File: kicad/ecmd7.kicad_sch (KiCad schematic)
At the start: 91 parts, among them J1 PMOD_SPI_ENC, J2 PMOD_ADC_MPIO, J3 PMOD_DRV, J4 Conn_01x02_Socket, J5 Encoder, J6 12V, J7 RS422/BISS-C, J8 5V, Q1 IRFS3806, Q11 MMBT3904, Q12 MMBT3904, Q2 IRFS3806, Q3 IRFS3806, Q4 IRFS3806, Q5 IRFS3806, Q6 IRFS3806, U1 TMC6200-TA

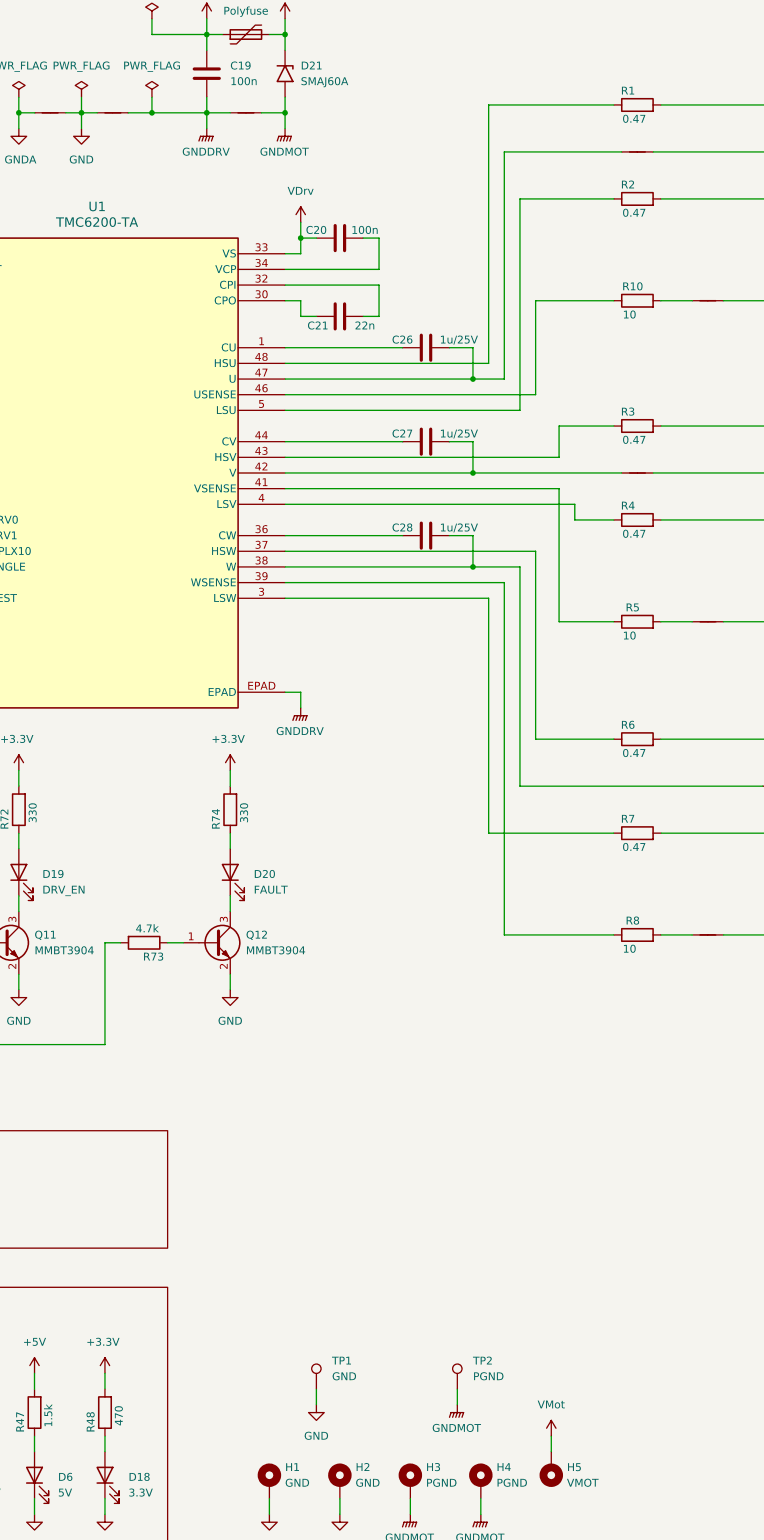
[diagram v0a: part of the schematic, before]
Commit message: Update project structure for enhancment with firmware and software
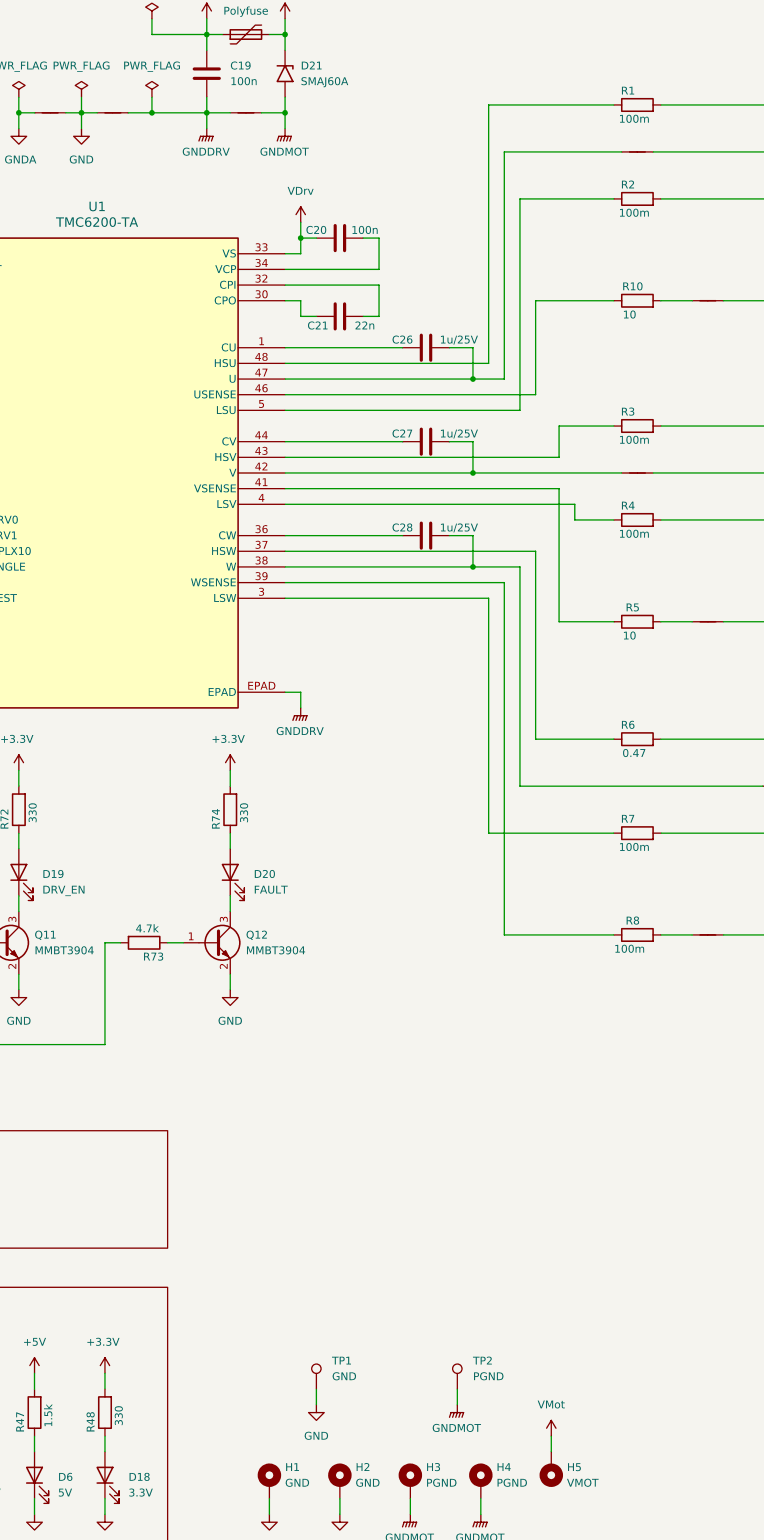
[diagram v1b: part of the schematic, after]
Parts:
- D21: Mouser Part Number (none) -> 576-SMAJ60A
- R1, R2, R3, R4, R7: value 0.47 -> 100m
- R48: value 470 -> 330
- R8: value 10 -> 100m
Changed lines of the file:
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@@
 			)
 		)
-		(property "Value" "0.47"
+		(property "Value" "100m"
 			(at 301.752 58.166 90)
 			(effects
@@
 			)
 		)
-		(property "Value" "0.47"
+		(property "Value" "100m"
 			(at 301.752 94.996 90)
 			(effects
@@
 			)
 		)
-		(property "Value" "0.47"
+		(property "Value" "100m"
 			(at 301.752 161.036 90)
 			(effects
@@
 			)
 		)
+		(property "Mouser Part Number" " 576-SMAJ60A"
+			(at 245.11 35.56 90)
+			(effects
+				(font
+					(size 1.27 1.27)
+				)
+				(hide yes)
+			)
+		)
 		(pin "1"
 		)
@@
 			)
 		)
-		(property "Value" "0.47"
+		(property "Value" "100m"
 			(at 301.752 42.926 90)
 			(effects
@@
 			)
 		)
-		(property "Value" "10"
+		(property "Value" "100m"
 			(at 300.99 177.546 90)
 			(effects
@@
 			)
 		)
-		(property "Value" "470"
+		(property "Value" "330"
 			(at 218.186 253.238 90)
 			(effects
@@
 			)
 		)
-		(property "Value" "0.47"
+		(property "Value" "100m"
 			(at 301.752 110.236 90)
 			(effects

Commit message: Cleanup schematic
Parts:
- removed C13, C14, C15, C16, C17, C18: 1n, Capacitor_SMD:C_0805_2012Metric, symbol Device:C
- removed C19, C20, C22, C25: 100n, Capacitor_SMD:C_0805_2012Metric, symbol Device:C
- removed C21: 22n, Capacitor_SMD:C_0805_2012Metric, symbol Device:C
- removed C23: 4.7u/25V, Capacitor_SMD:C_0805_2012Metric, symbol Device:C
- removed C24: 2.2u/25V, Capacitor_SMD:C_0805_2012Metric, symbol Device:C
- removed C26, C27, C28: 1u/25V, Capacitor_SMD:C_0805_2012Metric, symbol Device:C
- removed D18: 3.3V, Diode_SMD:D_0805_2012Metric, symbol Device:LED
- removed D19: DRV_EN, Diode_SMD:D_0805_2012Metric, symbol Device:LED
- removed D20: FAULT, Diode_SMD:D_0805_2012Metric, symbol Device:LED
- removed D21: SMAJ60A, Diode_SMD:D_SMA, symbol Diode:SMAJ60A
- removed D5: 12V, Diode_SMD:D_0805_2012Metric, symbol Device:LED
- removed D6: 5V, Diode_SMD:D_0805_2012Metric, symbol Device:LED
- removed F1: Polyfuse, Fuse:Fuse_0805_2012Metric, symbol Device:Polyfuse
- removed J6: 12V, Connector_PinSocket_2.54mm:PinSocket_1x02_P2.54mm_Vertical, symbol Connector:Conn_01x02_Socket
- removed J8: 5V, Connector_PinSocket_2.54mm:PinSocket_1x02_P2.54mm_Vertical, symbol Connector:Conn_01x02_Socket
- removed NTP2G1, NTP2G4: NetTie_2, NetTie:NetTie-2_SMD_Pad2.0mm, symbol Device:NetTie_2
- removed NTP2G2, NTPU1, NTPV1, NTPW1, NTSU1, NTSV1, NTSW1: NetTie_2, NetTie:NetTie-2_SMD_Pad0.5mm, symbol Device:NetTie_2
- removed Q1, Q2, Q3, Q4, Q5, Q6: IRFS3806, Package_TO_SOT_SMD:TO-263-2, symbol Transistor_FET:IRFS4115
- removed Q11, Q12: MMBT3904, Package_TO_SOT_SMD:SOT-23, symbol Transistor_BJT:MMBT3904
- removed R1, R2, R3, R4, R7, R8: 100m, Resistor_SMD:R_0805_2012Metric, symbol Device:R
- removed R10, R5: 10, Resistor_SMD:R_0805_2012Metric, symbol Device:R
- removed R46, R69, R73: 4.7k, Resistor_SMD:R_0805_2012Metric, symbol Device:R
- removed R47: 1.5k, Resistor_SMD:R_0805_2012Metric, symbol Device:R
- removed R48, R72, R74: 330, Resistor_SMD:R_0805_2012Metric, symbol Device:R
- removed R6: 0.47, Resistor_SMD:R_0805_2012Metric, symbol Device:R
- removed RU1, RV1, RW1: 15m, Resistor_SMD:R_0612_1632Metric, symbol Device:R
- removed TPU1: U, TestPoint:TestPoint_Loop_D2.50mm_Drill1.0mm, symbol Connector:TestPoint
- removed TPV1: V, TestPoint:TestPoint_Loop_D2.50mm_Drill1.0mm, symbol Connector:TestPoint
- removed TPW1: W, TestPoint:TestPoint_Loop_D2.50mm_Drill1.0mm, symbol Connector:TestPoint
- removed U1: TMC6200-TA, SSTA:eTQFP48_9x9_TRI, symbol SSTA:TMC6200-TA
- added C76: 100n, Capacitor_SMD:C_0805_2012Metric, symbol Device:C
- added JP10: ~{WP}=1, Jumper:SolderJumper-2_P1.3mm_Bridged_RoundedPad1.0x1.5mm, symbol Jumper:SolderJumper_2_Bridged
- added JP12: ~{WP}=0, Jumper:SolderJumper-2_P1.3mm_Open_RoundedPad1.0x1.5mm, symbol Jumper:SolderJumper_2_Open
- added R49, R53, R76, R9: 4.7k, Resistor_SMD:R_0805_2012Metric, symbol Device:R
- added U15: 74LVC1G139, Package_SO:SSOP-8_2.95x2.8mm_P0.65mm, symbol 74xGxx:74LVC1G139
- added U16: MB85RS1MT, Package_SO:SOP-8_3.76x4.96mm_P1.27mm, symbol Memory_NVRAM:MB85RS1MT
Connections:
- net +3.3V: now also C76.1, JP10.2 (B), R53.1, R9.1, U15.8 (VCC), U16.8 (VDD)
- net CS0: now also U15.1 (A)
- net CS1: now also U15.2 (B)
- net GND: now also C76.2, JP12.1 (A), R49.2, R76.2, U15.4 (GND), U16.4 (GND), U16.7 (~{HOLD})
- net SPI_SCK: now also R53.2, R76.1, U16.6 (SCK)
- net SPI_SDI: now also R49.1, R9.2, U16.5 (SI)
- net SPI_SDO: now also U16.2 (SO)
- net ~{CS_DRV}: now also U15.6 (Y1)
- net Power Stage/U: now reaches JU1.1 (Pin_1)
- net Power Stage/W: now reaches JW1.1 (Pin_1)
- net Power Stage/V: now reaches JV1.1 (Pin_1)
- new net: JP10.1 (A), JP12.2 (B), U16.3 (~{WP})
- new net ~{CS_FRAM}: U15.5 (Y2), U16.1 (~{CS})
- new net ~{CS_TMP}: U15.3 (Y3)
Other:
- sheet ADC+IO renamed ADC
- added sheet Power Stage (powerstage.kicad_sch)
- added sheet Sensors (sensors.kicad_sch)
- sheet ADC ports: added AD_SCK, AD_SDO_IU, AD_SDO_IV, AD_SDO_IW, AD_SDO_VBUS, I_U, I_V, I_W, ~{CS_AD}; removed none
- note added: "ABZ-Encoder Supply Selection"
- note added: "Battery/Power Connector"
- note added: "BiSS-C/RS422 Supply Selection"
- note added: "Control Connectors"
- note added: "Controller"
- note added: "Motor Terminals"
- note added: "SPI 2-to-4 CS Decoder"
- note added: "SPI FRAM (Nonvolatile Config Memory)"
- note added: "SPI Pseudo Termination"
- moved on the sheet: C42, C57, F2, F3, H1, H2, H3, H4, H5, J1, J2, J3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

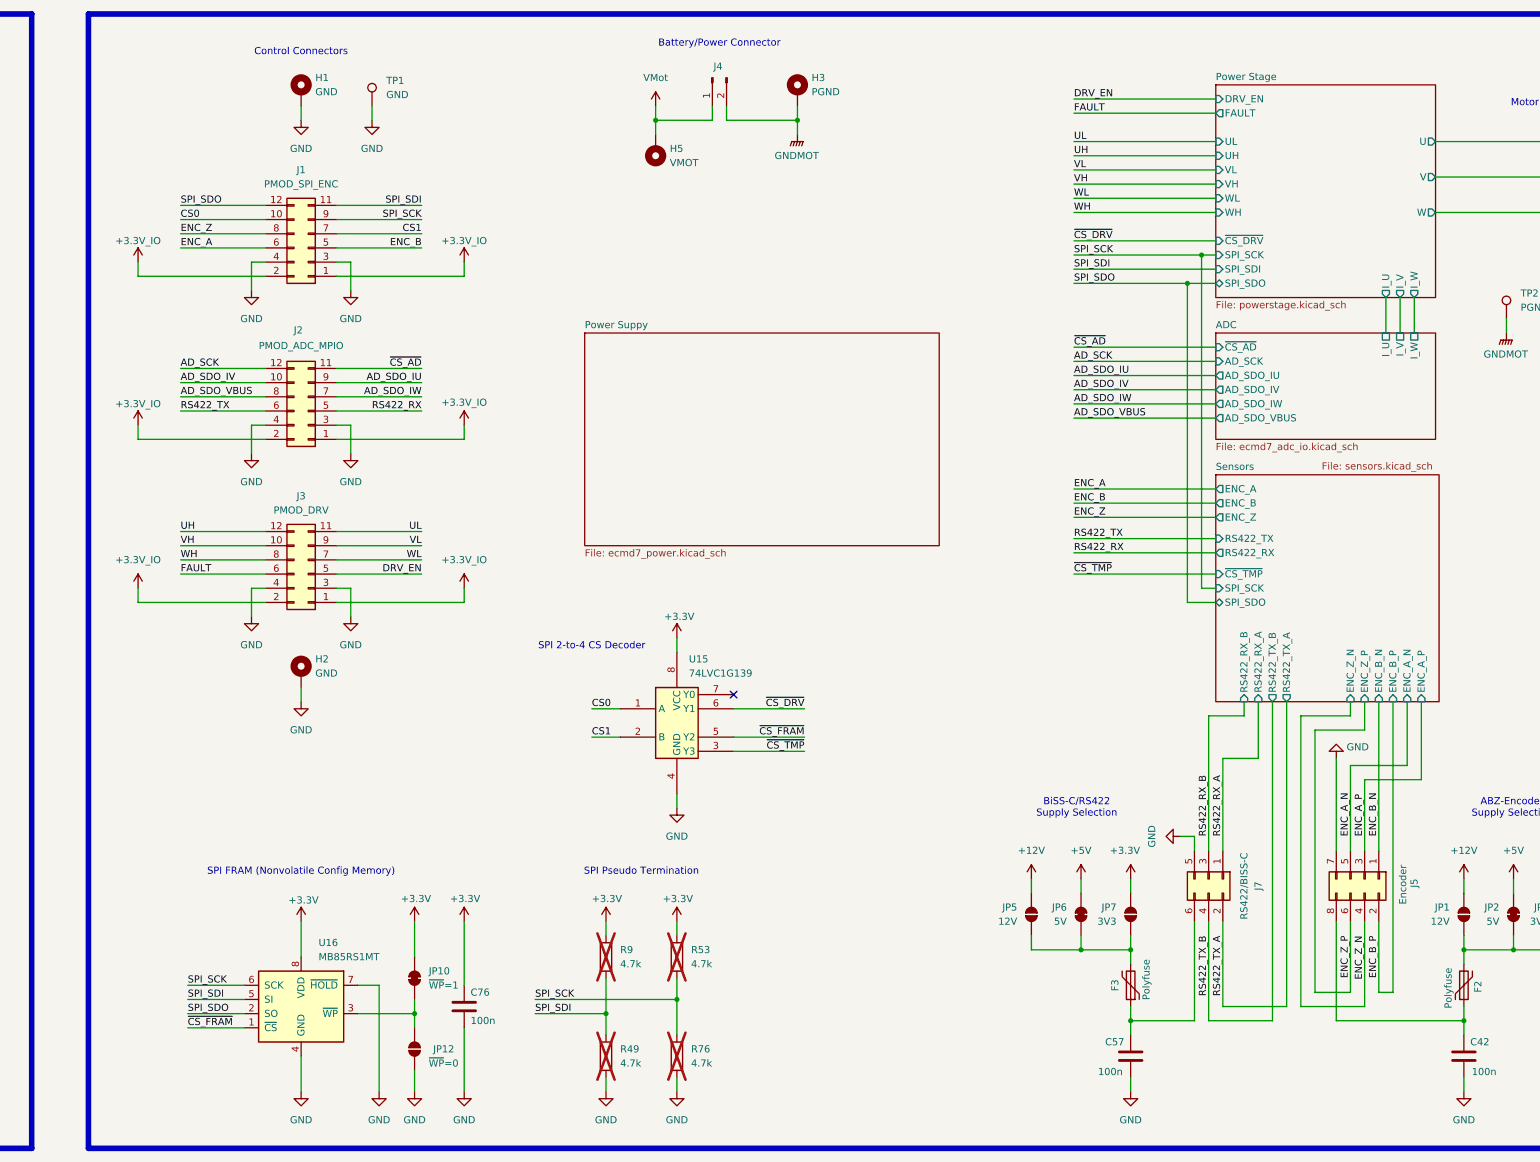
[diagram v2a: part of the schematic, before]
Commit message: Cleanup schematic, add busses
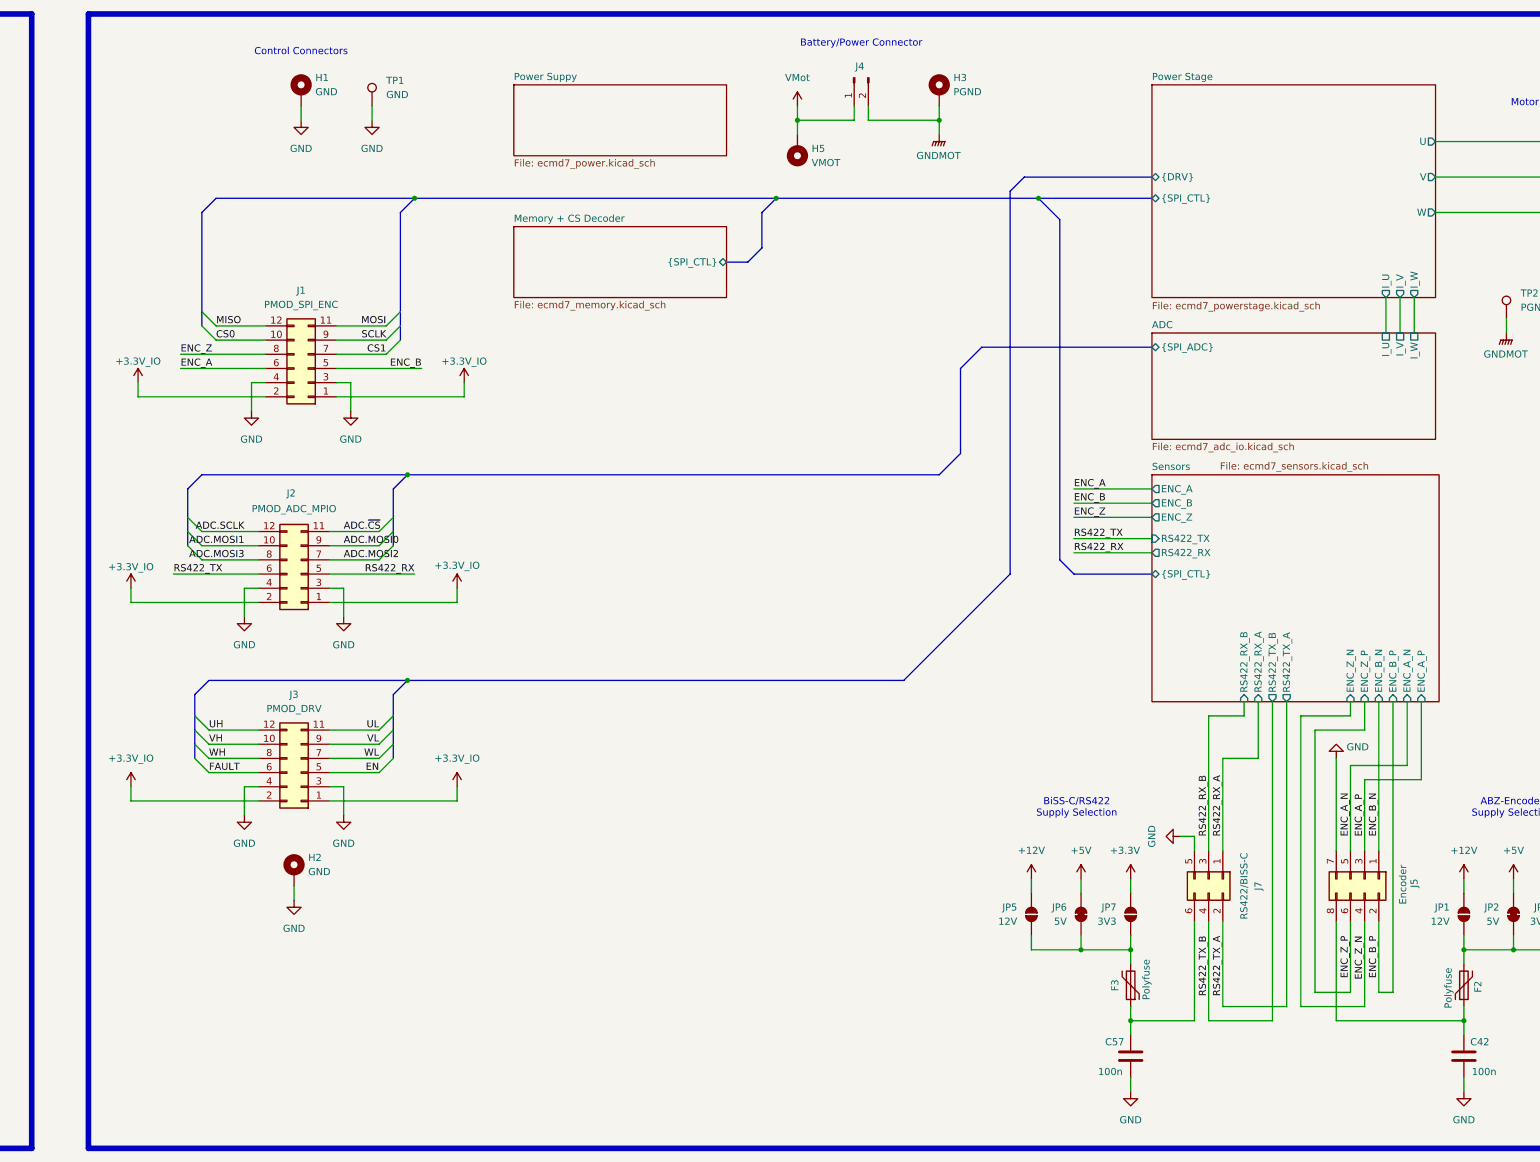
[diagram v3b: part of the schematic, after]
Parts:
- removed C76: 100n, Capacitor_SMD:C_0805_2012Metric, symbol Device:C
- removed JP10: ~{WP}=1, Jumper:SolderJumper-2_P1.3mm_Bridged_RoundedPad1.0x1.5mm, symbol Jumper:SolderJumper_2_Bridged
- removed JP12: ~{WP}=0, Jumper:SolderJumper-2_P1.3mm_Open_RoundedPad1.0x1.5mm, symbol Jumper:SolderJumper_2_Open
- removed R49, R53, R76, R9: 4.7k, Resistor_SMD:R_0805_2012Metric, symbol Device:R
- removed U15: 74LVC1G139, Package_SO:SSOP-8_2.95x2.8mm_P0.65mm, symbol 74xGxx:74LVC1G139
- removed U16: MB85RS1MT, Package_SO:SOP-8_3.76x4.96mm_P1.27mm, symbol Memory_NVRAM:MB85RS1MT
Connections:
- net AD_SCK renamed ADC.SCLK
- net AD_SDO_IU renamed ADC.MOSI0
- net AD_SDO_IV renamed ADC.MOSI1
- net AD_SDO_IW renamed ADC.MOSI2
- net AD_SDO_VBUS renamed ADC.MOSI3
- net DRV_EN renamed EN
- net SPI_SCK renamed SCLK
- net SPI_SDI renamed MOSI
- net SPI_SDO renamed MISO
- net ~{CS_AD} renamed ADC.~{CS}
- no-connect marks 1 -> 0
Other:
- added sheet Memory + CS Decoder (ecmd7_memory.kicad_sch)
- sheet ADC ports: added {SPI_ADC}; removed AD_SCK, AD_SDO_IU, AD_SDO_IV, AD_SDO_IW, AD_SDO_VBUS, ~{CS_AD}
- sheet Power Stage: file powerstage.kicad_sch -> ecmd7_powerstage.kicad_sch
- sheet Power Stage ports: added {DRV}, {SPI_CTL}; removed DRV_EN, FAULT, SPI_SCK, SPI_SDI, SPI_SDO, UH, UL, VH, VL, WH, WL, ~{CS_DRV}
- sheet Sensors: file sensors.kicad_sch -> ecmd7_sensors.kicad_sch
- sheet Sensors ports: added {SPI_CTL}; removed SPI_SCK, SPI_SDO, ~{CS_TMP}
- note removed: "SPI 2-to-4 CS Decoder"
- note removed: "SPI FRAM (Nonvolatile Config Memory)"
- note removed: "SPI Pseudo Termination"
- moved on the sheet: H2, H3, H5, J1, J2, J3, J4
